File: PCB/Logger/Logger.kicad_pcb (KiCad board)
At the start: 2 copper layers, 70 x 70 mm, 68 parts, among them J1 JST-PH-SM4-TB, J2 USB-C-Socket-V, J3 Conn_01x05, J4 Shelly, J5 USB-PROG, J6 TF_PUSH, Q1 CJ2301, Q2 C179347, U1 ESP32-S3-MINI-1, U3 TP4054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

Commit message: SS
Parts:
- C2: footprint Capacitor_Tantalum_SMD:CP_EIA-7343-31_Kemet-D -> RevK:CP_EIA-7343-31_Kemet-D

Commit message: Tidy
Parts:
- moved C19 0.10 mm to (95.6, 94.4)
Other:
- board text added: "C"
- board text added: "S"

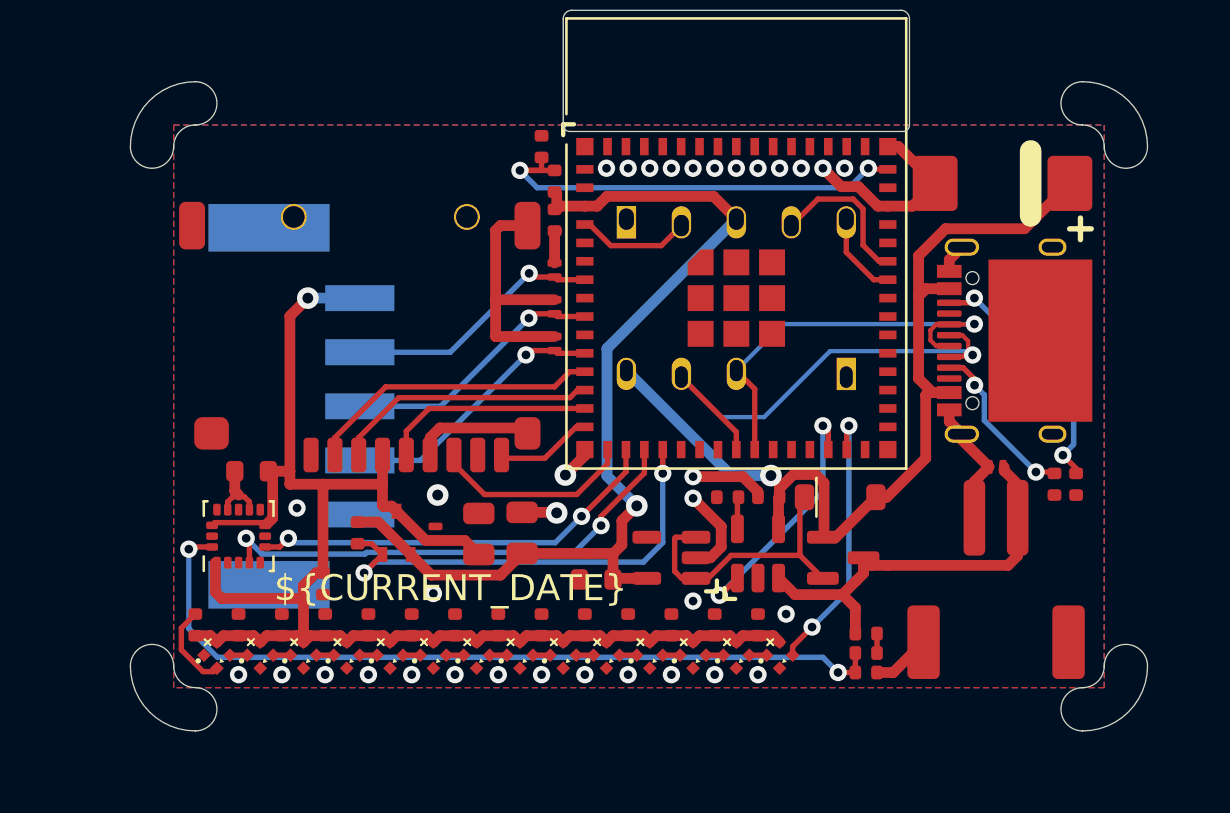
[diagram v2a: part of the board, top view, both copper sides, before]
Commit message: Reworked, more LEDs, etc
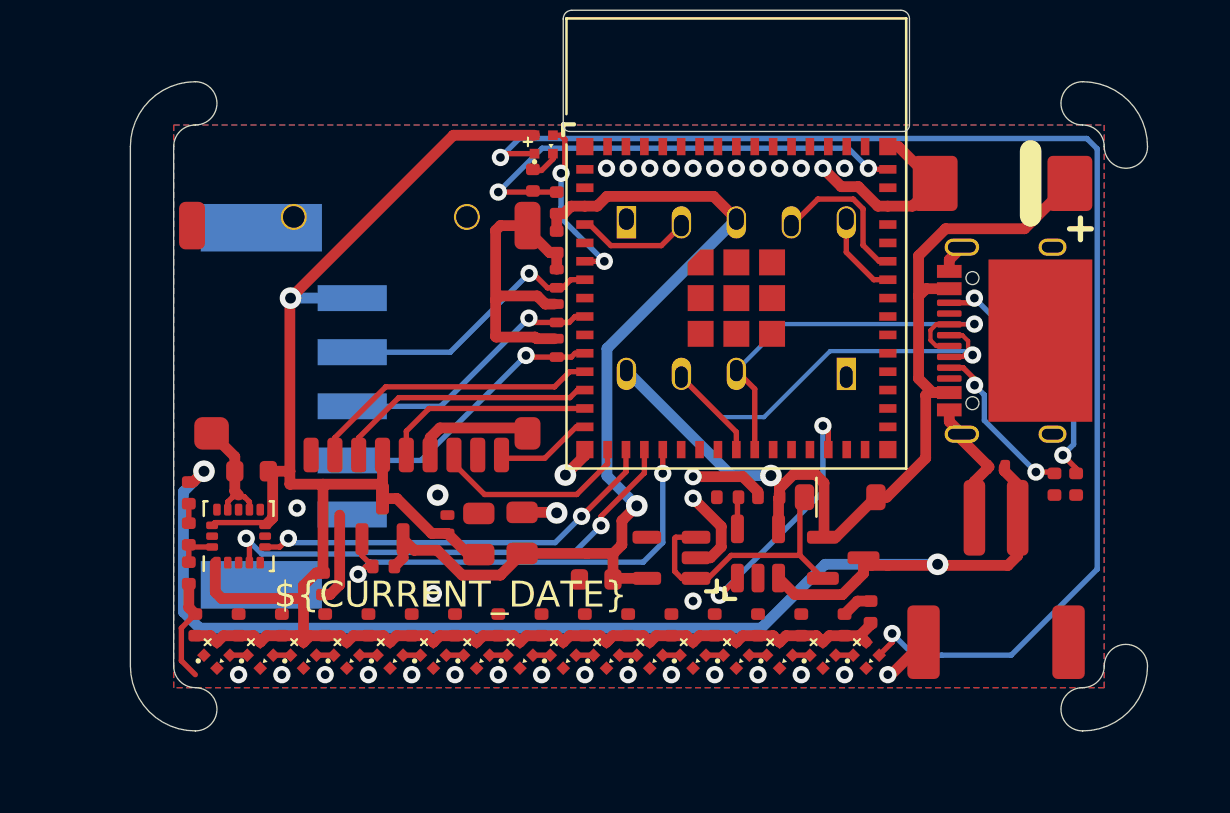
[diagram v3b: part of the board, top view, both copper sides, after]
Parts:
- removed V3: ~, RevK:VCUT70N
- added C23: 100nF, RevK:C_0402, F.Cu at (83.0, 113.1)
- added C24: 100nF, RevK:C_0402, F.Cu at (81.0, 113.1)
- added C25: 100nF, RevK:C_0402, F.Cu at (79.0, 113.1)
- added D21: XL-1010RGBC-WS2812B, RevK:SMD1010, F.Cu at (84.0, 114.5)
- added D22: XL-1010RGBC-WS2812B, RevK:SMD1010, F.Cu at (82.0, 114.5)
- added D23: XL-1010RGBC-WS2812B, RevK:SMD1010, F.Cu at (80.0, 114.5)
- Q2: footprint RevK:SOT-323_SC-70 -> RevK:SOT-23
- moved R9 32.0 mm to (78.7, 107.0), turned to -90 degrees
- moved R7 31.8 mm to (78.7, 108.9), turned to -90 degrees
- moved R8 31.6 mm to (78.7, 110.7), turned to -90 degrees
- moved D4 26.0 mm to (95.1, 90.9), turned to 90 degrees
- moved C10 6.00 mm to (99.0, 113.1)
- moved C11 6.00 mm to (97.0, 113.1)
- moved C12 6.00 mm to (95.0, 113.1)
- moved C13 6.00 mm to (93.0, 113.1)
- moved C14 6.00 mm to (91.0, 113.1)
- moved C15 6.00 mm to (89.0, 113.1)
- moved C16 6.00 mm to (87.0, 113.1)
- moved C17 6.00 mm to (85.0, 113.1)
- moved C4 6.00 mm to (109.0, 113.1)
- moved C6 6.00 mm to (107.0, 113.1)
- moved C7 6.00 mm to (105.0, 113.1)
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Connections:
- D1 pad 2: GPSRX -> GPSTX
- D19 pad 1: unconnected-(D19-O-Pad1) -> Net-(D19-O)
- D3 pad 2: GPSTX -> GPSRX
- J3 pad 2: GPSRX -> GPSTX
- J3 pad 3: GPSTX -> GPSRX
- U1 pad 11: GPSRX -> GPSTX
- U1 pad 29: RGB -> unconnected-(U1-GPIO34-Pad29)
- U1 pad 6: unconnected-(U1-GPIO2-Pad6) -> RGB
- U1 pad 9: GPSTX -> GPSRX
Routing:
- net Net-(D4-O): track 0.80 -> 62.0 mm, vias 0 -> 2
- net VBAT: track 17.7 -> 59.8 mm, vias 0 -> 2
- net ADC: track 37.3 -> 1.92 mm, vias 2 -> 0
- net SPWR: track 73.8 -> 93.0 mm
- net GND: track 56.4 -> 67.5 mm, vias 34 -> 36
- net RGB: track 12.8 -> 8.07 mm
- net Net-(U1-EN): track 20.9 -> 21.9 mm
- net +3.3V: track 44.8 -> 43.8 mm
- net Net-(D22-O): track 0.00 -> 0.80 mm
- net Net-(D21-O): track 0.00 -> 0.80 mm
- net Net-(D19-O): track 0.00 -> 0.80 mm
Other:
- board text added: "2 3 5 7 8 9 10 11 12 13 14 15 33"
- board text added: "RGB GPSTICK GPSRX GPSTX SDSS SDMOSI SDSCK SDCD SDMISO ACCSDA ACCSCL PWR STAT"
- board text removed: "3 5 7 8 9 10 11 12 13 14 15 33 34"
- board text removed: "GPSTICK GPSTX GPSRX SDSS SDMOSI SDSCK SDCD SDMISO ACCSDA ACCSCL PWR STAT RGB"

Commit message: More caps
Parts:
- added C26: 100uF, RevK:C_0805, F.Cu at (112.8, 106.0)
- C1, C18: value 4.7uF/50V -> 100uF
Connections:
- C2 pad 1: VBUS -> +3.3V
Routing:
- net +3.3V: track 43.8 -> 61.9 mm, vias 1 -> 2
- net VBUS: track 44.4 -> 33.9 mm
- net GND: track 67.5 -> 69.9 mm
